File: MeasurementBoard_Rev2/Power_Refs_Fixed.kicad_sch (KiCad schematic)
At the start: 11 parts, among them U3 ADR4530, U4 ADA4807-2ACP, U5 ADP7118-1.8

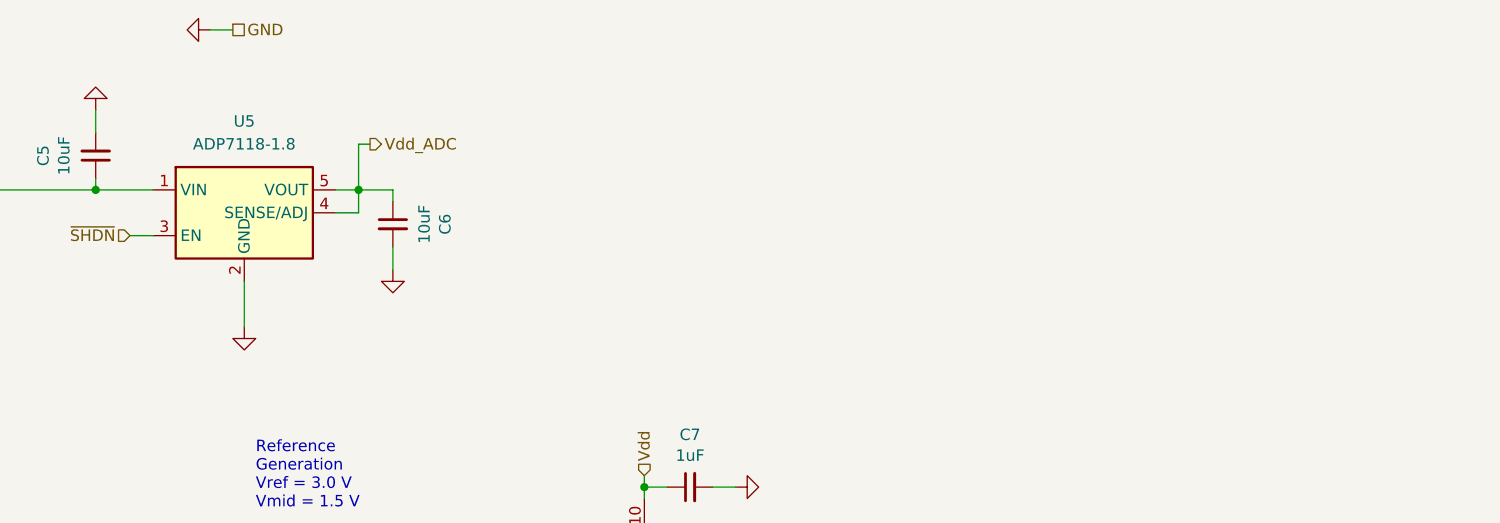
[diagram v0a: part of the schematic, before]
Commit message: Finished Measurement Board Update Minus Heater Board Connections
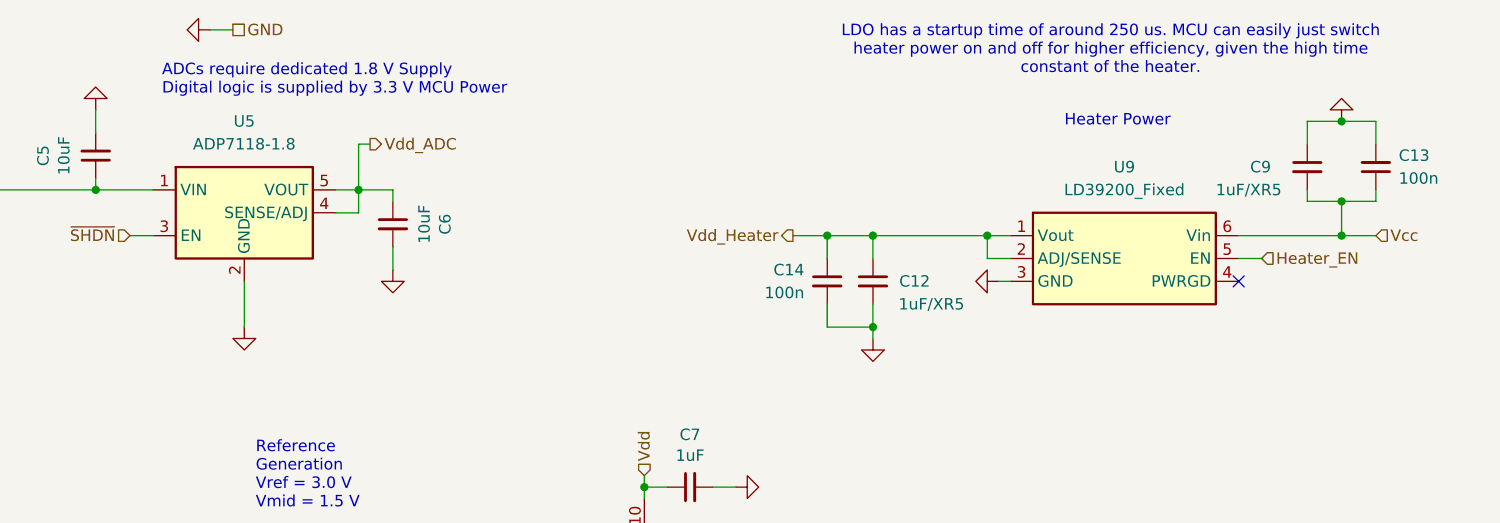
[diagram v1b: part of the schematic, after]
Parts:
- added C12, C9: 1uF/XR5, Capacitor_SMD:C_0603_1608Metric_Pad1.08x0.95mm_HandSolder, symbol Device:C_Small
- added C13, C14: 100n, Capacitor_SMD:C_0603_1608Metric_Pad1.08x0.95mm_HandSolder, symbol Device:C_Small
- added U9: LD39200_Fixed, Package_DFN_QFN:DFN-6-1EP_3x3mm_P0.95mm_EP1.7x2.6mm, symbol FrontEndPrototype_Rev1-rescue:LD39200_Fixed
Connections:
- net GND: now also C12.2, C13.2, C14.2, C9.1, U9.3 (GND)
- new net Heater_EN: U9.5 (EN)
- new net Vcc: C13.1, C9.2, U9.6 (Vin)
- new net Vdd_Heater: C12.1, C14.1, U9.1 (Vout), U9.2 (ADJ/SENSE)
- no-connect marks 0 -> 1
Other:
- note added: "ADCs require dedicated 1.8 V Supply Digital logic is supplied by 3.3 V MCU Power"
- note added: "Heater Power"
- note added: "LDO has a startup time of around 250 us. MCU can easily just switch heater power on and off for higher efficiency, given the high time constant of the heater."

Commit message: Finished Measurement Board Fixes Schematic and PCB
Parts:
- added C19, C22: 100n, Capacitor_SMD:C_0603_1608Metric_Pad1.08x0.95mm_HandSolder, symbol Device:C_Small
- added C20, C21: 1uF/XR5, Capacitor_SMD:C_0603_1608Metric_Pad1.08x0.95mm_HandSolder, symbol Device:C_Small
- added Q1: SSM3J358R, Package_TO_SOT_SMD:SOT-23-3, symbol FrontEndPrototype_Rev1-rescue:SSM3J358R
- added U1: LD39200_Fixed, Package_DFN_QFN:DFN-6-1EP_3x3mm_P0.95mm_EP1.7x2.6mm, symbol FrontEndPrototype_Rev1-rescue:LD39200_Fixed
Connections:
- net GND: now also C19.2, C20.2, C21.1, C22.2, U1.3 (GND)
- net Vcc: now also C21.2, C22.1, U1.6 (Vin)
- net Heater_EN: no longer names the net of U9.5 (EN)
- net Vdd_Heater: no longer names the net of C12.1, C14.1, U9.1 (Vout), U9.2 (ADJ/SENSE)
- net Vdd_Heater: now also Q1.2 (S)
- new net 3V3: C19.1, C20.1, U1.1 (Vout), U1.2 (ADJ/SENSE)
- new net Heater_OUT: Q1.3 (D)
- new net Heater_PWM: Q1.1 (G)
- no-connect marks 1 -> 2
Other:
- note added: "Main Power"

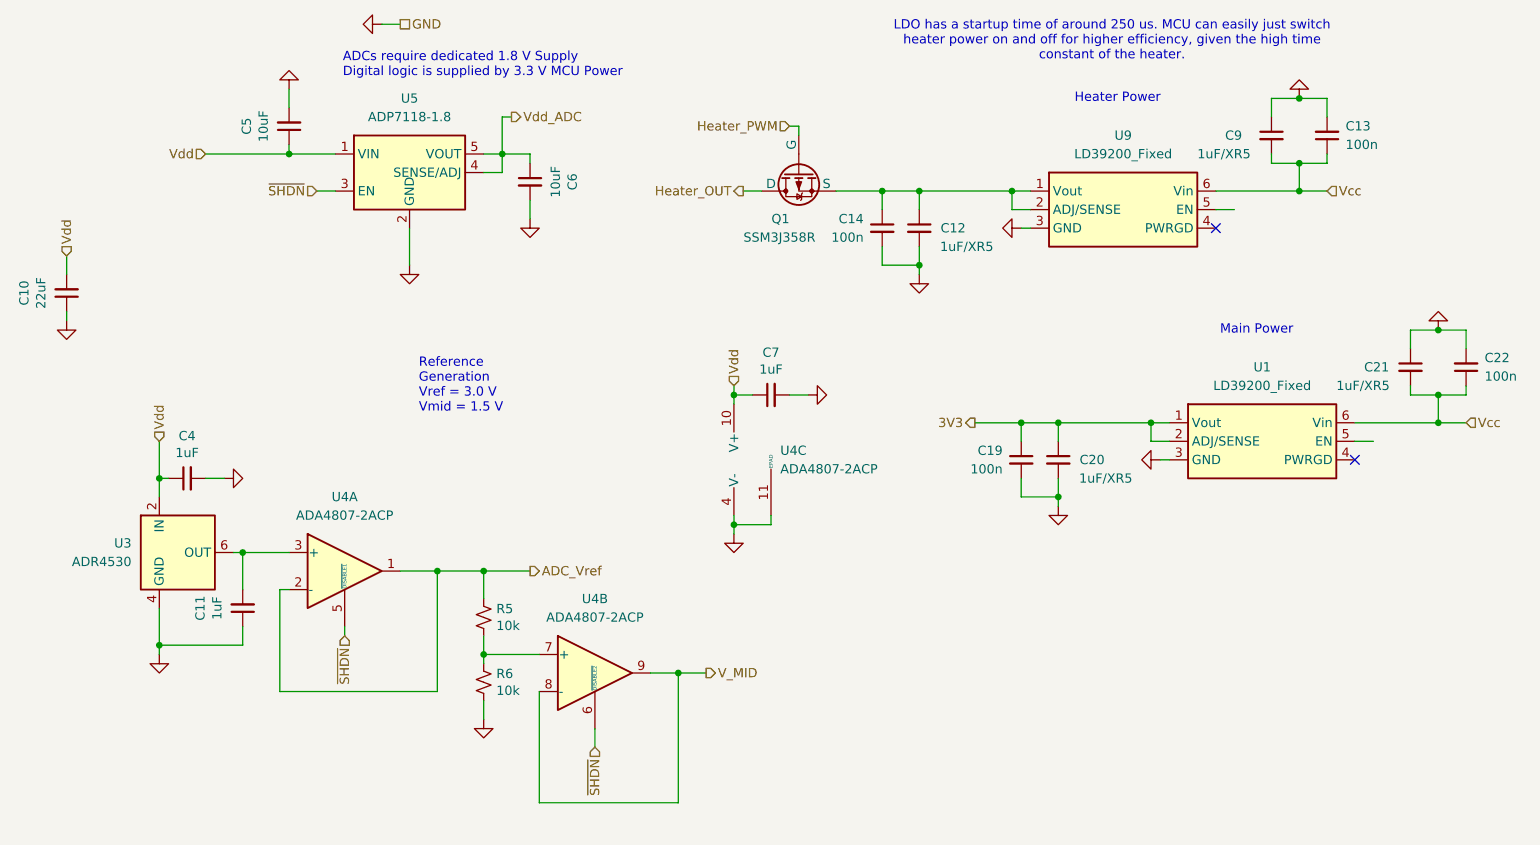
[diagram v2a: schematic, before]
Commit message: Updated Measurement Board with new 3V Reference
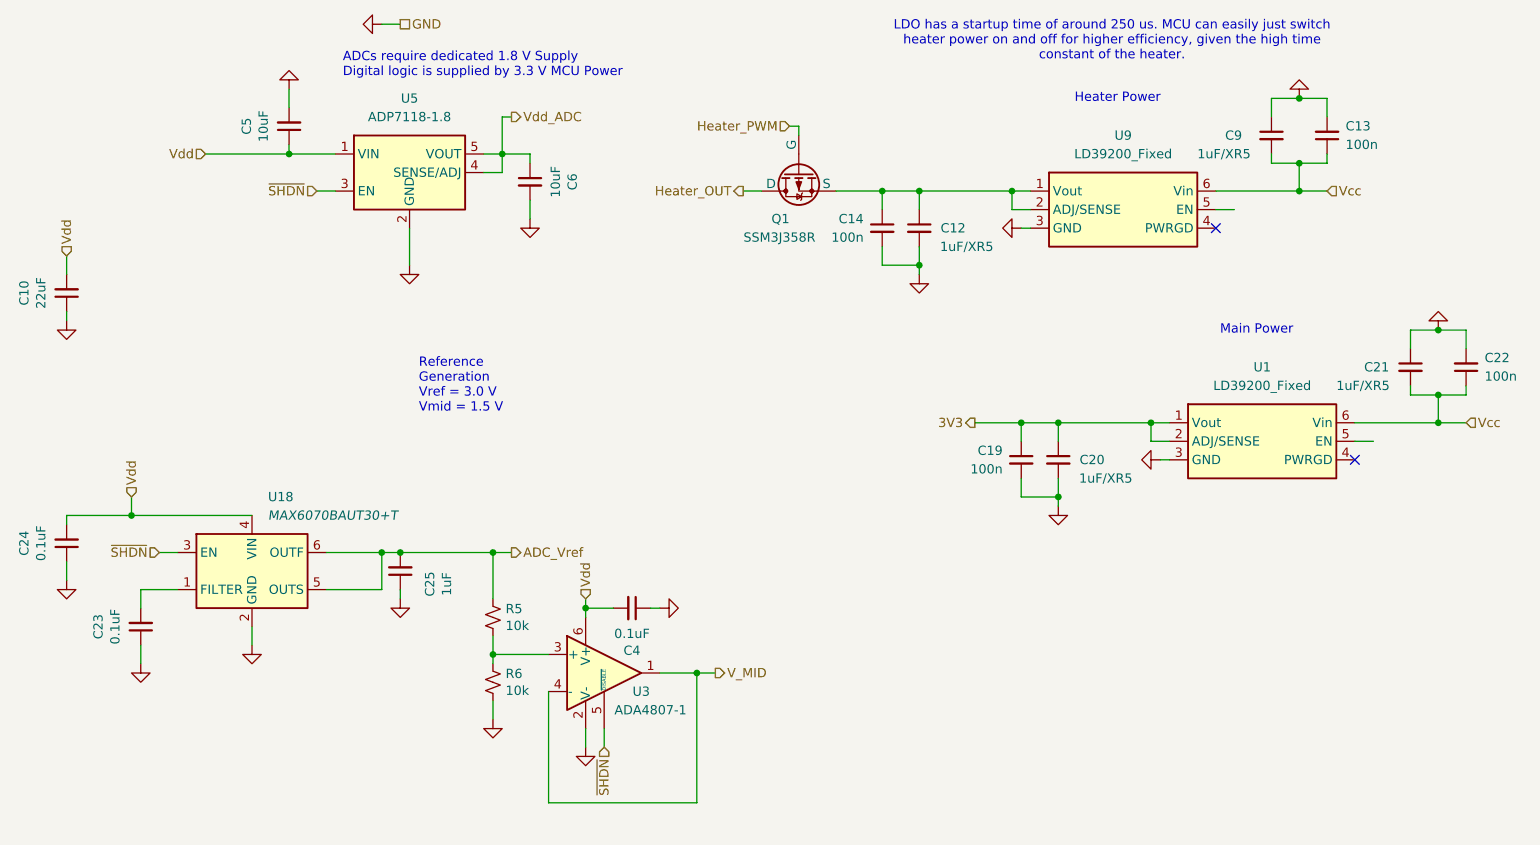
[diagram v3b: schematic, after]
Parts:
- removed C11, C7: 1uF, Capacitor_SMD:C_0603_1608Metric_Pad1.08x0.95mm_HandSolder, symbol Device:C_Small
- removed U3: ADR4530, Package_SO:SOIC-8_3.9x4.9mm_P1.27mm, symbol Reference_Voltage:ADR4530
- removed U4: ADA4807-2ACP, Package_CSP:LFCSP-WD-10-1EP_3x3mm_P0.5mm_EP1.64x2.38mm, symbol Amplifier_Operational:ADA4807-2ACP
- added C23, C24: 0.1uF, Capacitor_SMD:C_0603_1608Metric_Pad1.08x0.95mm_HandSolder, symbol Device:C_Small
- added C25: 1uF, Capacitor_SMD:C_0603_1608Metric_Pad1.08x0.95mm_HandSolder, symbol Device:C_Small
- added U18: MAX6070BAUT30+T, Package_TO_SOT_SMD:SOT-23-6, symbol Reference_Voltage:MAX6070BAUT30+T
- added U3: ADA4807-1, Package_TO_SOT_SMD:SOT-23-6_Handsoldering, symbol Amplifier_Operational:ADA4807-1
- C4: value 1uF -> 0.1uF
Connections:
- net ADC_Vref: now also C25.2, U18.5 (OUTS), U18.6 (OUTF)
- net GND: now also C4.1, C23.1, C24.1, C25.1, U18.2 (GND), U3.2 (V-); no longer C4.2
- net V_MID: now also U3.1, U3.4 (-)
- net Vdd: now also C4.2, C24.2, U18.4 (VIN), U3.6 (V+); no longer C4.1
- net ~{SHDN}: now also U18.3 (EN), U3.5 (~{DISABLE})
- net at R5.2, R6.1: now also U3.3 (+)
- new net: C23.2, U18.1 (FILTER)
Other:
- moved on the sheet: R5, R6

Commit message: Final Edit Before Check and Combine
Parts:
- added F1: 250mA Fast-Blow, Fuse:Fuse_0603_1608Metric_Pad1.05x0.95mm_HandSolder, symbol Device:Fuse_Small
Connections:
- net 3V3: now also F1.1; no longer C19.1, C20.1, U1.1 (Vout), U1.2 (ADJ/SENSE)
- new net: C19.1, C20.1, F1.2, U1.1 (Vout), U1.2 (ADJ/SENSE)
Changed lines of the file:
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@@
 	(wire
 		(pts
-			(xy 153.67 81.28) (xy 160.02 81.28)
+			(xy 137.16 81.28) (xy 143.51 81.28)
 		)
 		(stroke
@@
 		(pts
 			(xy 29.21 66.04) (xy 29.21 67.31)
+		)
+		(stroke
+			(width 0)
+			(type default)
+		)
+	)
+	(wire
+		(pts
+			(xy 148.59 81.28) (xy 160.02 81.28)
 		)
 		(stroke
@@
 	(hierarchical_label "3V3"
 		(shape output)
-		(at 153.67 81.28 180)
+		(at 137.16 81.28 180)
 		(fields_autoplaced yes)
 		(effects
@@
 					(unit 1)
 				)
+			)
+		)
+	)
+	(symbol
+		(lib_id "Device:Fuse_Small")
+		(at 146.05 81.28 0)
+		(unit 1)
+		(exclude_from_sim no)
+		(in_bom yes)
+		(on_board yes)
+		(dnp no)
+		(fields_autoplaced yes)
+		(property "Reference" "F1"
+			(at 146.05 76.2 0)
+			(effects
+				(font
+					(size 1.27 1.27)
+				)
+			)
+		)
+		(property "Value" "250mA Fast-Blow"
+			(at 146.05 78.74 0)
+			(effects
+				(font
+					(size 1.27 1.27)
+				)
+			)
+		)
+		(property "Footprint" "Fuse:Fuse_0603_1608Metric_Pad1.05x0.95mm_HandSolder"
+			(at 146.05 81.28 0)
+			(effects
+				(font
+					(size 1.27 1.27)
+				)
+				(hide yes)
+			)
+		)
+		(property "Datasheet" "~"
+			(at 146.05 81.28 0)
+			(effects
+				(font
+					(size 1.27 1.27)
+				)
+				(hide yes)
+			)
+		)
+		(property "Description" "Fuse, small symbol"
+			(at 146.05 81.28 0)
+			(effects
+				(font
+					(size 1.27 1.27)
+				)
+				(hide yes)
+			)
+		)
+		(pin "1"
+		)
+		(pin "2"
+		)
+		(instances
+			(project ""
+				(path "/5bbe1190-7cf9-4e92-afa2-f39bae3944d2/b559fc21-9388-4421-af70-eeb8bfb4b138"
+					(reference "F1")
+					(unit 1)
+				)

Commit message: Final Rev3 Commit Post Submission
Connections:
- net Vcc: now also U1.5 (EN), U9.5 (EN)
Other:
- moved on the sheet: C25
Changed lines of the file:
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@@
 	)
 	(junction
+		(at 162.56 91.44)
+		(diameter 0)
+		(color 0 0 0 0)
+	)
+	(junction
 		(at 72.39 99.06)
 		(diameter 0)
@@
 	)
 	(junction
+		(at 189.23 49.53)
+		(diameter 0)
+		(color 0 0 0 0)
+	)
+	(junction
 		(at 158.75 49.53)
 		(diameter 0)
@@
 	)
 	(junction
-		(at 165.1 91.44)
+		(at 208.28 81.28)
 		(diameter 0)
 		(color 0 0 0 0)
@@
 	(wire
 		(pts
+			(xy 162.56 91.44) (xy 165.1 91.44)
+		)
+		(stroke
+			(width 0)
+			(type default)
+		)
+	)
+	(wire
+		(pts
 			(xy 165.1 81.28) (xy 177.8 81.28)
 		)
@@
 	(wire
 		(pts
-			(xy 165.1 91.44) (xy 165.1 92.71)
+			(xy 162.56 91.44) (xy 162.56 92.71)
 		)
 		(stroke
@@
 	(wire
 		(pts
-			(xy 160.02 91.44) (xy 165.1 91.44)
+			(xy 160.02 91.44) (xy 162.56 91.44)
 		)
 		(stroke
@@
 	(wire
 		(pts
+			(xy 189.23 49.53) (xy 189.23 52.07)
+		)
+		(stroke
+			(width 0)
+			(type default)
+		)
+	)
+	(wire
+		(pts
 			(xy 95.25 118.11) (xy 95.25 133.35)
 		)
@@
 	(wire
 		(pts
-			(xy 74.93 104.14) (xy 74.93 105.41)
+			(xy 208.28 81.28) (xy 208.28 83.82)
 		)
 		(stroke
@@
 	(wire
 		(pts
+			(xy 74.93 106.68) (xy 74.93 105.41)
+		)
+		(stroke
+			(width 0)
+			(type default)
+		)
+	)
+	(wire
+		(pts
 			(xy 100.33 123.19) (xy 100.33 125.73)
 		)
@@
 	(wire
 		(pts
-			(xy 186.69 49.53) (xy 198.12 49.53)
+			(xy 186.69 49.53) (xy 189.23 49.53)
 		)
 		(stroke
@@
 	(wire
 		(pts
+			(xy 208.28 81.28) (xy 217.17 81.28)
+		)
+		(stroke
+			(width 0)
+			(type default)
+		)
+	)
+	(wire
+		(pts
 			(xy 48.26 44.45) (xy 59.69 44.45)
 		)
@@
 	(wire
 		(pts
+			(xy 74.93 100.33) (xy 74.93 99.06)
+		)
+		(stroke
+			(width 0)
+			(type default)
+		)
+	)
+	(wire
+		(pts
 			(xy 41.91 99.06) (xy 44.45 99.06)
 		)
@@
 	(wire
 		(pts
+			(xy 189.23 49.53) (xy 198.12 49.53)
+		)
+		(stroke
+			(width 0)
+			(type default)
+		)
+	)
+	(wire
+		(pts
 			(xy 160.02 83.82) (xy 160.02 81.28)
 		)
@@
 	(wire
 		(pts
-			(xy 76.2 54.61) (xy 76.2 59.69)
+			(xy 76.2 54.61) (xy 76.2 57.15)
 		)
 		(stroke
@@
 	(wire
 		(pts
-			(xy 205.74 81.28) (xy 217.17 81.28)
+			(xy 205.74 81.28) (xy 208.28 81.28)
 		)
 		(stroke
@@
 	(symbol
 		(lib_id "power:GND")
-		(at 76.2 59.69 0)
+		(at 76.2 57.15 0)
 		(unit 1)
 		(exclude_from_sim no)
@@
 		(dnp no)
 		(property "Reference" "#PWR018"
-			(at 76.2 66.04 0)
+			(at 76.2 63.5 0)
 			(effects
 				(font
@@
 		)
 		(property "Value" "GND"
-			(at 76.327 62.9412 90)
+			(at 76.327 60.4012 90)
 			(effects
 				(font
@@
 		)
 		(property "Footprint" ""
-			(at 76.2 59.69 0)
+			(at 76.2 57.15 0)
 			(effects
 				(font
@@
 		)
 		(property "Datasheet" ""
-			(at 76.2 59.69 0)
+			(at 76.2 57.15 0)
 			(effects
 				(font
@@
 		)
 		(property "Description" ""
-			(at 76.2 59.69 0)
+			(at 76.2 57.15 0)
 			(effects
 				(font
@@
 	(symbol
 		(lib_id "power:GND")
-		(at 165.1 92.71 0)
+		(at 162.56 92.71 0)
 		(mirror y)
 		(unit 1)
@@
 		(dnp no)
 		(property "Reference" "#PWR043"
-			(at 165.1 99.06 0)
+			(at 162.56 99.06 0)
 			(effects
 				(font
@@
 		)
 		(property "Value" "GND"
-			(at 167.64 91.44 90)
+			(at 165.1 91.44 90)
 			(effects
 				(font
@@
 		)
 		(property "Footprint" ""
-			(at 165.1 92.71 0)
+			(at 162.56 92.71 0)
 			(effects
 				(font
@@
 		)
 		(property "Datasheet" ""
-			(at 165.1 92.71 0)
+			(at 162.56 92.71 0)
 			(effects
 				(font
@@
 		)
 		(property "Description" ""
-			(at 165.1 92.71 0)
+			(at 162.56 92.71 0)
 			(effects
 				(font
@@
 	(symbol
 		(lib_id "Device:C_Small")
-		(at 74.93 101.6 180)
+		(at 74.93 102.87 180)
 		(unit 1)
 		(exclude_from_sim no)
@@
 		(dnp no)
 		(property "Reference" "C25"
-			(at 78.994 103.378 90)
+			(at 78.994 104.648 90)
 			(effects
 				(font
@@
 		)
 		(property "Value" "1uF"
-			(at 81.3054 103.378 90)
+			(at 81.3054 104.648 90)
 			(effects
 				(font
@@
 		)
 		(property "Footprint" "Capacitor_SMD:C_0603_1608Metric_Pad1.08x0.95mm_HandSolder"
-			(at 74.93 101.6 0)
+			(at 74.93 102.87 0)
 			(effects
 				(font
@@
 		)
 		(property "Datasheet" "~"
-			(at 74.93 101.6 0)
+			(at 74.93 102.87 0)
 			(effects
 				(font
@@
 		)
 		(property "Description" ""
-			(at 74.93 101.6 0)
+			(at 74.93 102.87 0)
 			(effects
 				(font
@@
 	(symbol
 		(lib_id "power:GND")
-		(at 74.93 105.41 0)
+		(at 74.93 106.68 0)
 		(unit 1)
 		(exclude_from_sim no)
@@
 		(dnp no)
 		(property "Reference" "#PWR078"
-			(at 74.93 111.76 0)
+			(at 74.93 113.03 0)
 			(effects
 				(font
@@
 		)
 		(property "Value" "GND"
-			(at 75.057 108.6612 90)
+			(at 75.057 109.9312 90)
 			(effects
 				(font
@@
 		)
 		(property "Footprint" ""
-			(at 74.93 105.41 0)
+			(at 74.93 106.68 0)
 			(effects
 				(font
@@
 		)
 		(property "Datasheet" ""
-			(at 74.93 105.41 0)
+			(at 74.93 106.68 0)
 			(effects
 				(font
@@
 		)
 		(property "Description" ""
-			(at 74.93 105.41 0)
+			(at 74.93 106.68 0)
 			(effects
 				(font
